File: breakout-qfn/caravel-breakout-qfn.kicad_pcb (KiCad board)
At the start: 2 copper layers, 45 x 57.5 mm, 83 parts, among them CON1 FH-00339, CON2 FH-00339, CON3 73251-1352, U1 Caravel_QFN

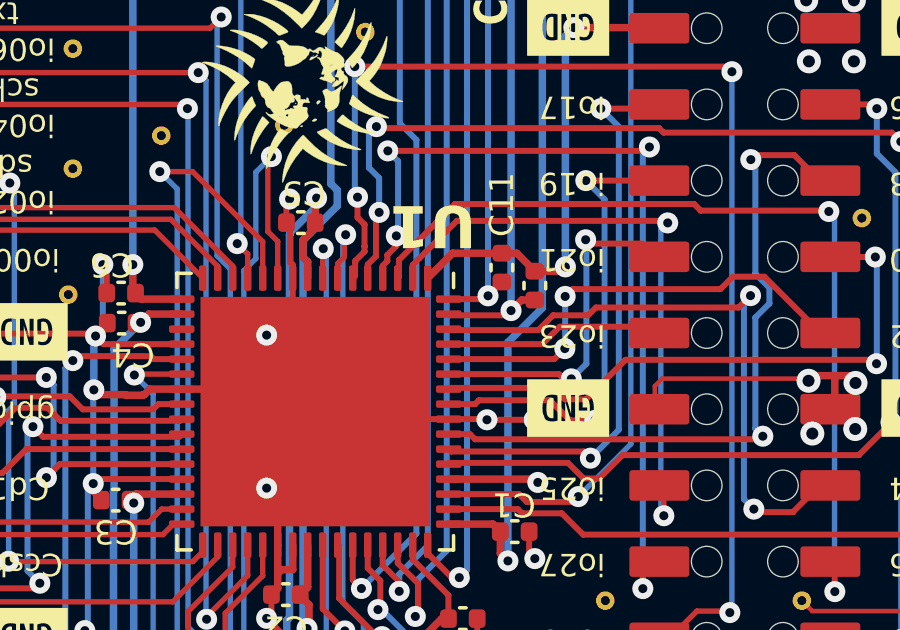
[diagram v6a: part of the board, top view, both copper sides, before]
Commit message: QFN breakout sanity naming for nets
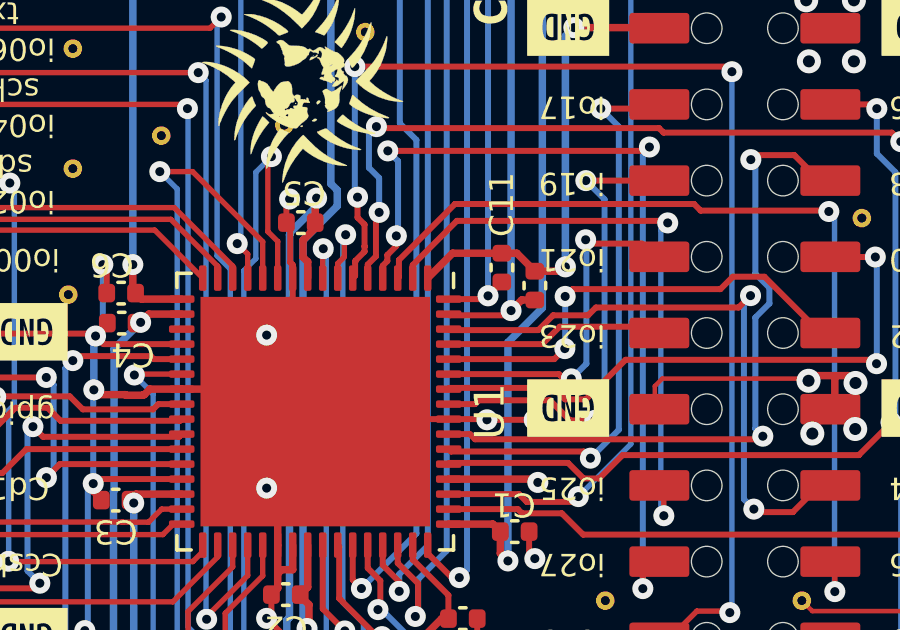
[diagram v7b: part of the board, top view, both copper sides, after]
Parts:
- CON1, CON2: value FH-00339 -> REF-182665-01
- U1: value Caravel_QFN -> Caravel_QFN_TT4; footprint Package_DFN_QFN:QFN-64-1EP_9x9mm_P0.5mm_EP7.65x7.65mm -> TinyTapeout:QFN-64-1EP_9x9mm_P0.5mm_EP7.65x7.65mm_REDUCEDPASTE
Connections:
- net mprj_io[0] renamed JTAG/mio[0]
- net mprj_io[10] renamed ui_in[2]/mio[10]
- net mprj_io[11] renamed ui_in[3]/mio[11]
- net mprj_io[12] renamed ui_in[4]/mio[12]
- net mprj_io[13] renamed ui_in[5]/mio[13]
- net mprj_io[14] renamed ui_in[6]/mio[14]
- net mprj_io[15] renamed ui_in[7]/mio[15]
- net mprj_io[16] renamed uo_out[0]/mio[16]
- net mprj_io[17] renamed uo_out[1]/mio[17]
- net mprj_io[18] renamed uo_out[2]/mio[18]
- net mprj_io[19] renamed uo_out[3]/mio[19]
- net mprj_io[1]_SDO renamed SDO/mio[1]
- net mprj_io[20] renamed uo_out[4]/mio[20]
- net mprj_io[21] renamed uo_out[5]/mio[21]
- net mprj_io[22] renamed uo_out[6]/mio[22]
- net mprj_io[23] renamed uo_out[7]/mio[23]
- net mprj_io[24] renamed uio[0]/mio[24]
- net mprj_io[25] renamed uio[1]/mio[25]
- net mprj_io[26] renamed uio[2]/mio[26]
- net mprj_io[27] renamed uio[3]/mio[27]
- net mprj_io[28] renamed uio[4]/mio[28]
- net mprj_io[29] renamed uio[5]/mio[29]
- net mprj_io[2]_SDI renamed SDI/mio[2]
- net mprj_io[30] renamed uio[6]/mio[30]
- net mprj_io[31] renamed uio[7]/mio[31]
- net mprj_io[32] renamed ctrl_ena/mio[32]
- net mprj_io[33] renamed mio[33]
- net mprj_io[34] renamed ctrl_sel_inc/mio[34]
- net mprj_io[35] renamed mio[35]
- net mprj_io[36] renamed ~{ctrl_sel_rst}/mio[36]
- net mprj_io[37] renamed mio[37]
- net mprj_io[3]_CSB renamed CSB/mio[3]
- net mprj_io[4]_SCK renamed SCK/mio[4]
- net mprj_io[5]_ser_rx renamed usrclk2/mio[5]
- net mprj_io[6]_ser_tx renamed clk/mio[6]
- net mprj_io[7] renamed ~{rst}/mio[7]
- net mprj_io[8] renamed ui_in[0]/mio[8]
- net mprj_io[9] renamed ui_in[1]/mio[9]

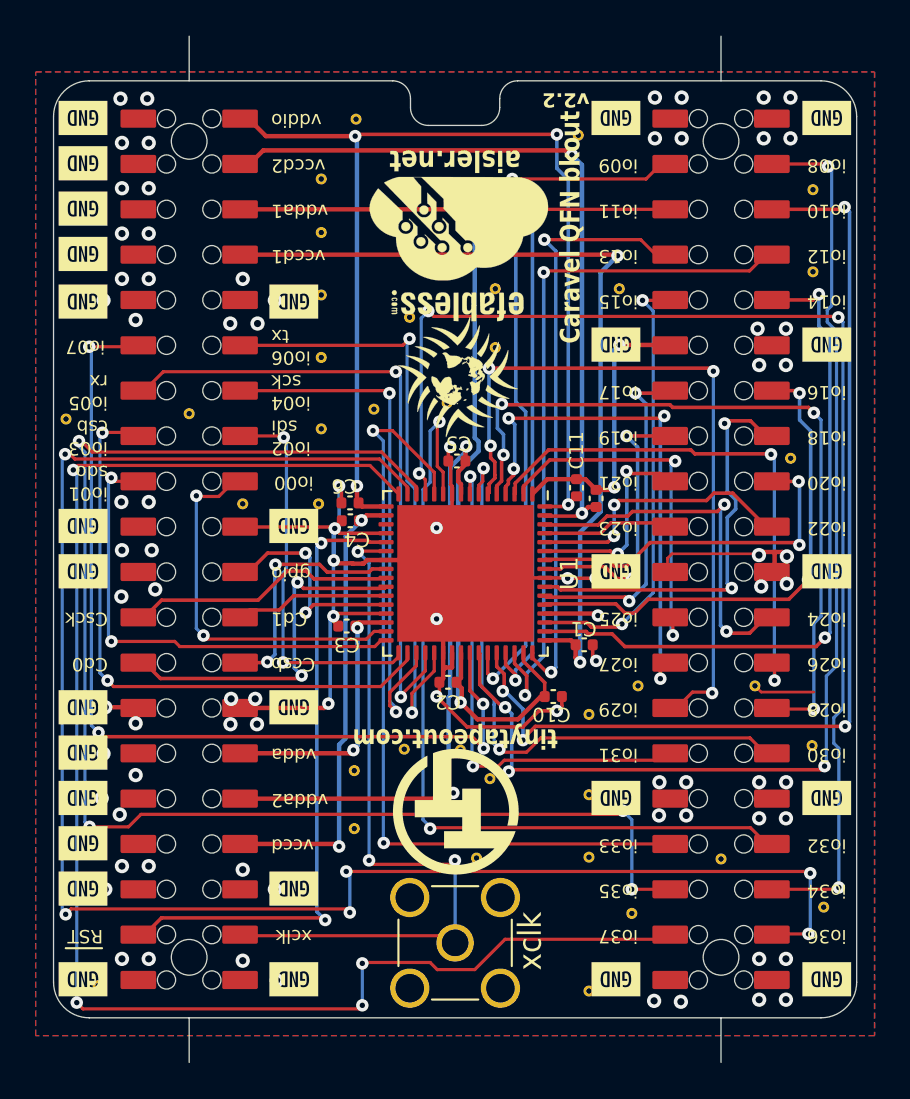
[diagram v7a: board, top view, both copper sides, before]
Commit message: v3.0, breaking changes for ultra-goodness: EMC,TT pinout, FPGA
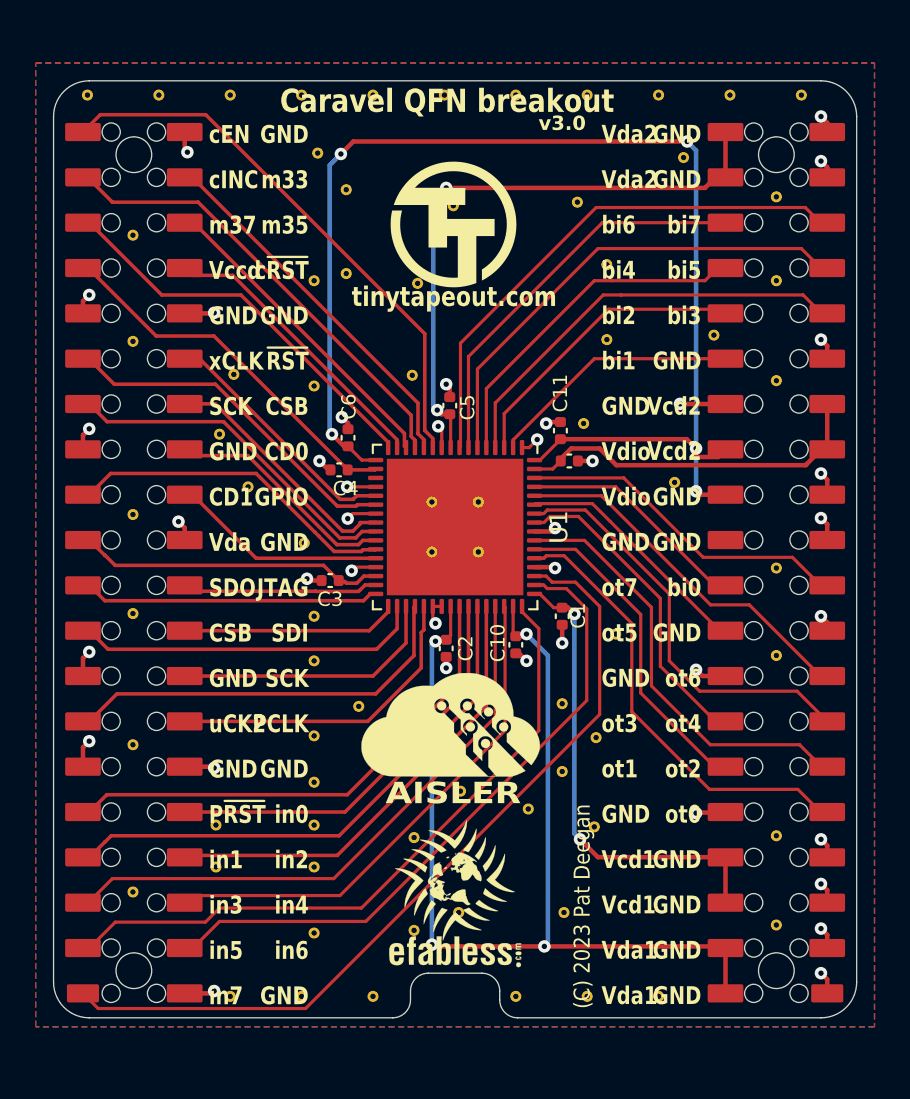
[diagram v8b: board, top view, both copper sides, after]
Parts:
- removed CON3: 73251-1352, ok-connectors:TE_5-1814832-2
- removed the REF** at (90.5, 54.8)
- removed the REF** at (72.8, 32.5)
- removed the REF** at (65.0, 19.6)
- removed the REF** at (63.0, 37.0)
- removed the REF** at (63.0, 33.0)
- removed the REF** at (50.5, 68.2)
- removed the REF** at (85.4, 61.1)
- removed the REF** at (64.8, 56.1)
- removed the REF** at (63.0, 26.0)
- removed the REF** at (67.7, 55.0)
- removed the REF** at (89.3, 38.6)
- removed the REF** at (90.5, 23.6)
- removed the REF** at (87.3, 51.4)
- removed the REF** at (90.5, 28.2)
- removed the REF** at (64.8, 59.4)
- removed the REF** at (48.7, 36.5)
- removed the REF** at (63.0, 23.0)
- removed the REF** at (55.6, 36.1)
- removed the REF** at (77.4, 20.6)
- removed the REF** at (78.0, 53.0)
- removed the REF** at (72.8, 29.1)
- removed the REF** at (80.4, 64.2)
- removed the REF** at (71.7, 61.0)
- removed the REF** at (78.0, 57.5)
- removed the REF** at (66.0, 35.9)
- removed the REF** at (62.9, 41.2)
- removed the REF** at (78.0, 68.5)
- removed the REF** at (68.0, 30.8)
- removed the REF** at (63.0, 29.5)
- removed the REF** at (80.8, 51.4)
- removed the REF** at (70.0, 35.5)
- removed the REF** at (79.7, 29.1)
- removed the REF** at (78.0, 61.0)
- removed the REF** at (58.6, 41.2)
- removed the REF** at (72.5, 56.6)
- removed the REF** at (72.8, 24.4)
- removed the REF** at (91.2, 63.8)
- removed the REF** at (70.8, 55.0)
- removed kibuzzard-6288F08E (x28): G***, kibuzzard-6288F08E
- added G***: LOGO, flyingcarsfootprints:PsychoLogoSmall, B.Cu at (70.5, 24.1)
- added REF**: Z2A_logo, Logos:Z2A_logo, B.Cu at (64.2, 58.7)
- added REF**: TT_logo, Logos:TT_logo, B.Cu at (78.8, 59.0)
- added STITCH1: StitchingVia-0.3mm, flyingcarsfootprints:StitchingVia-0.3mm, F.Cu at (69.2, 43.9)
- added STITCH1: StitchingVia-0.3mm, flyingcarsfootprints:StitchingVia-0.3mm, F.Cu at (76.6, 64.1)
- added STITCH1: StitchingVia-0.3mm, flyingcarsfootprints:StitchingVia-0.3mm, F.Cu at (78.3, 59.3)
- added STITCH1: StitchingVia-0.3mm, flyingcarsfootprints:StitchingVia-0.3mm, F.Cu at (71.8, 41.1)
- added STITCH1: StitchingVia-0.3mm, flyingcarsfootprints:StitchingVia-0.3mm, F.Cu at (70.7, 64.1)
- added STITCH1: StitchingVia-0.3mm, flyingcarsfootprints:StitchingVia-0.3mm, F.Cu at (83.3, 21.8)
- added STITCH1: StitchingVia-0.3mm, flyingcarsfootprints:StitchingVia-0.3mm, F.Cu at (70.4, 24.5)
- added STITCH1: StitchingVia-0.3mm, flyingcarsfootprints:StitchingVia-0.3mm, F.Cu at (69.2, 41.1)
- added STITCH1: StitchingVia-0.3mm, flyingcarsfootprints:StitchingVia-0.3mm, F.Cu at (49.9, 18.3)
- added STITCH1: StitchingVia-0.3mm, flyingcarsfootprints:StitchingVia-0.3mm, F.Cu at (71.8, 43.9)
- added STITCH1: StitchingVia-0.3mm, flyingcarsfootprints:StitchingVia-0.3mm, F.Cu at (64.4, 22.6)
- added STITCH10: StitchingVia-0.3mm, flyingcarsfootprints:StitchingVia-0.3mm, F.Cu at (85.9, 18.3)
- added STITCH11: StitchingVia-0.3mm, flyingcarsfootprints:StitchingVia-0.3mm, F.Cu at (89.9, 18.3)
- added STITCH12: StitchingVia-0.3mm, flyingcarsfootprints:StitchingVia-0.3mm, F.Cu at (61.9, 68.8)
- added STITCH13: StitchingVia-0.3mm, flyingcarsfootprints:StitchingVia-0.3mm, F.Cu at (65.9, 68.8)
- added STITCH15: StitchingVia-0.3mm, flyingcarsfootprints:StitchingVia-0.3mm, F.Cu at (73.9, 68.8)
- added STITCH16: StitchingVia-0.3mm, flyingcarsfootprints:StitchingVia-0.3mm, F.Cu at (77.9, 68.8)
- added STITCH17: StitchingVia-0.3mm, flyingcarsfootprints:StitchingVia-0.3mm, F.Cu at (74.6, 58.3)
- added STITCH17: StitchingVia-0.3mm, flyingcarsfootprints:StitchingVia-0.3mm, F.Cu at (52.5, 26.1)
- added STITCH17: StitchingVia-0.3mm, flyingcarsfootprints:StitchingVia-0.3mm, F.Cu at (77.3, 24.3)
- added STITCH17: StitchingVia-0.3mm, flyingcarsfootprints:StitchingVia-0.3mm, F.Cu at (68.4, 28.9)
- added STITCH17: StitchingVia-0.3mm, flyingcarsfootprints:StitchingVia-0.3mm, F.Cu at (78.4, 54.3)
- added STITCH17: StitchingVia-0.3mm, flyingcarsfootprints:StitchingVia-0.3mm, F.Cu at (68.2, 65.1)
- added STITCH17: StitchingVia-0.3mm, flyingcarsfootprints:StitchingVia-0.3mm, F.Cu at (76.5, 52.4)
- added STITCH17: StitchingVia-0.3mm, flyingcarsfootprints:StitchingVia-0.3mm, F.Cu at (68.1, 34.0)
- added STITCH17: StitchingVia-0.3mm, flyingcarsfootprints:StitchingVia-0.3mm, F.Cu at (58.9, 40.2)
- added STITCH17: StitchingVia-0.3mm, flyingcarsfootprints:StitchingVia-0.3mm, F.Cu at (62.6, 54.2)
- added STITCH17: StitchingVia-0.3mm, flyingcarsfootprints:StitchingVia-0.3mm, F.Cu at (52.5, 54.7)
- added STITCH17: StitchingVia-0.3mm, flyingcarsfootprints:StitchingVia-0.3mm, F.Cu at (70.8, 57.3)
- added STITCH17: StitchingVia-0.3mm, flyingcarsfootprints:StitchingVia-0.3mm, F.Cu at (52.5, 63.0)
- added STITCH17: StitchingVia-0.3mm, flyingcarsfootprints:StitchingVia-0.3mm, F.Cu at (79.0, 27.8)
- added STITCH17: StitchingVia-0.3mm, flyingcarsfootprints:StitchingVia-0.3mm, F.Cu at (74.4, 53.8)
- added STITCH17: StitchingVia-0.3mm, flyingcarsfootprints:StitchingVia-0.3mm, F.Cu at (57.1, 59.2)
- added STITCH17: StitchingVia-0.3mm, flyingcarsfootprints:StitchingVia-0.3mm, F.Cu at (62.6, 56.8)
- added STITCH17: StitchingVia-0.3mm, flyingcarsfootprints:StitchingVia-0.3mm, F.Cu at (88.5, 64.8)
- added STITCH17: StitchingVia-0.3mm, flyingcarsfootprints:StitchingVia-0.3mm, F.Cu at (52.5, 47.4)
- added STITCH17: StitchingVia-0.3mm, flyingcarsfootprints:StitchingVia-0.3mm, F.Cu at (88.5, 59.8)
- added STITCH17: StitchingVia-0.3mm, flyingcarsfootprints:StitchingVia-0.3mm, F.Cu at (52.5, 32.1)
- added STITCH17: StitchingVia-0.3mm, flyingcarsfootprints:StitchingVia-0.3mm, F.Cu at (88.5, 49.7)
- added STITCH17: StitchingVia-0.3mm, flyingcarsfootprints:StitchingVia-0.3mm, F.Cu at (68.2, 59.9)
- added STITCH17: StitchingVia-0.3mm, flyingcarsfootprints:StitchingVia-0.3mm, F.Cu at (62.6, 34.6)
- added STITCH17: StitchingVia-0.3mm, flyingcarsfootprints:StitchingVia-0.3mm, F.Cu at (62.6, 61.5)
- added STITCH17: StitchingVia-0.3mm, flyingcarsfootprints:StitchingVia-0.3mm, F.Cu at (62.6, 59.2)
- added STITCH17: StitchingVia-0.3mm, flyingcarsfootprints:StitchingVia-0.3mm, F.Cu at (62.6, 47.5)
- added STITCH17: StitchingVia-0.3mm, flyingcarsfootprints:StitchingVia-0.3mm, F.Cu at (65.1, 52.5)
- added STITCH17: StitchingVia-0.3mm, flyingcarsfootprints:StitchingVia-0.3mm, F.Cu at (77.7, 36.7)
- added STITCH17: StitchingVia-0.3mm, flyingcarsfootprints:StitchingVia-0.3mm, F.Cu at (82.8, 40.0)
- added STITCH17: StitchingVia-0.3mm, flyingcarsfootprints:StitchingVia-0.3mm, F.Cu at (62.6, 50.0)
- added STITCH17: StitchingVia-0.3mm, flyingcarsfootprints:StitchingVia-0.3mm, F.Cu at (64.4, 28.3)
- added STITCH17: StitchingVia-0.3mm, flyingcarsfootprints:StitchingVia-0.3mm, F.Cu at (79.0, 32.0)
- added STITCH17: StitchingVia-0.3mm, flyingcarsfootprints:StitchingVia-0.3mm, F.Cu at (58.1, 34.0)
- added STITCH17: StitchingVia-0.3mm, flyingcarsfootprints:StitchingVia-0.3mm, F.Cu at (88.5, 24.0)
- added STITCH17: StitchingVia-0.3mm, flyingcarsfootprints:StitchingVia-0.3mm, F.Cu at (79.5, 48.5)
- added STITCH17: StitchingVia-0.3mm, flyingcarsfootprints:StitchingVia-0.3mm, F.Cu at (88.5, 34.3)
- added STITCH17: StitchingVia-0.3mm, flyingcarsfootprints:StitchingVia-0.3mm, F.Cu at (62.8, 21.6)
- added STITCH17: StitchingVia-0.3mm, flyingcarsfootprints:StitchingVia-0.3mm, F.Cu at (57.1, 61.5)
- added STITCH17: StitchingVia-0.3mm, flyingcarsfootprints:StitchingVia-0.3mm, F.Cu at (52.5, 41.8)
- added STITCH17: StitchingVia-0.3mm, flyingcarsfootprints:StitchingVia-0.3mm, F.Cu at (88.5, 44.8)
- added STITCH17: StitchingVia-0.3mm, flyingcarsfootprints:StitchingVia-0.3mm, F.Cu at (85.0, 31.8)
- added STITCH17: StitchingVia-0.3mm, flyingcarsfootprints:StitchingVia-0.3mm, F.Cu at (57.3, 37.3)
- added STITCH17: StitchingVia-0.3mm, flyingcarsfootprints:StitchingVia-0.3mm, F.Cu at (76.5, 56.2)
- added STITCH17: StitchingVia-0.3mm, flyingcarsfootprints:StitchingVia-0.3mm, F.Cu at (62.6, 28.7)
- added STITCH17: StitchingVia-0.3mm, flyingcarsfootprints:StitchingVia-0.3mm, F.Cu at (81.9, 68.8)
- added STITCH17: StitchingVia-0.3mm, flyingcarsfootprints:StitchingVia-0.3mm, F.Cu at (62.6, 65.2)
- added STITCH17: StitchingVia-0.3mm, flyingcarsfootprints:StitchingVia-0.3mm, F.Cu at (88.5, 28.7)
- added STITCH17: StitchingVia-0.3mm, flyingcarsfootprints:StitchingVia-0.3mm, F.Cu at (62.0, 43.4)
- added STITCH17: StitchingVia-0.3mm, flyingcarsfootprints:StitchingVia-0.3mm, F.Cu at (68.2, 52.4)
- added STITCH2: StitchingVia-0.3mm, flyingcarsfootprints:StitchingVia-0.3mm, F.Cu at (53.9, 18.3)
- added STITCH3: StitchingVia-0.3mm, flyingcarsfootprints:StitchingVia-0.3mm, F.Cu at (57.9, 18.3)
- added STITCH3: StitchingVia-0.3mm, flyingcarsfootprints:StitchingVia-0.3mm, F.Cu at (57.9, 68.8)
- added STITCH4: StitchingVia-0.3mm, flyingcarsfootprints:StitchingVia-0.3mm, F.Cu at (61.9, 18.3)
- added STITCH5: StitchingVia-0.3mm, flyingcarsfootprints:StitchingVia-0.3mm, F.Cu at (65.9, 18.3)
- added STITCH6: StitchingVia-0.3mm, flyingcarsfootprints:StitchingVia-0.3mm, F.Cu at (69.9, 18.3)
- added STITCH7: StitchingVia-0.3mm, flyingcarsfootprints:StitchingVia-0.3mm, F.Cu at (73.9, 18.3)
- added STITCH8: StitchingVia-0.3mm, flyingcarsfootprints:StitchingVia-0.3mm, F.Cu at (77.9, 18.3)
- added STITCH9: StitchingVia-0.3mm, flyingcarsfootprints:StitchingVia-0.3mm, F.Cu at (81.9, 18.3)
- moved REF** 36.2 mm to (70.5, 66.3), turned to 0 degrees
- moved REF** 33.6 mm to (70.5, 56.5), turned to 0 degrees
- moved REF** 32.8 mm to (70.5, 25.6), turned to 0 degrees
- moved REF** 28.2 mm to (70.5, 62.3), turned to 0 degrees
- moved C6 3.65 mm to (64.5, 37.5), turned to -90 degrees
- moved C10 3.58 mm to (73.9, 49.1), turned to -90 degrees
- moved C11 3.32 mm to (76.4, 37.1)
- moved CON1 3.19 mm to (52.5, 44.5)
- moved CON2 3.19 mm to (88.5, 44.5)
- moved C5 3.13 mm to (70.2, 35.7), turned to -90 degrees
- moved C4 2.92 mm to (64.0, 39.3)
- moved C3 2.71 mm to (63.5, 45.5)
- moved U1 2.66 mm to (70.5, 42.5)
- moved C7 2.58 mm to (76.9, 38.8), turned to 180 degrees
- moved C1 2.02 mm to (76.5, 47.5), turned to 90 degrees
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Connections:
- CON1 pad 1: GND -> ctrl_ena/mio[32]
- CON1 pad 11: ~{rst}/mio[7] -> xclk
- CON1 pad 12: clk/mio[6] -> ~{RST}
- CON1 pad 13: usrclk2/mio[5] -> Caravel_SCK
- CON1 pad 14: SCK/mio[4] -> Caravel_CSB
- CON1 pad 15: CSB/mio[3] -> GND
- CON1 pad 16: SDI/mio[2] -> Caravel_D0
- CON1 pad 17: SDO/mio[1] -> Caravel_D1
- CON1 pad 18: JTAG/mio[0] -> gpio
- CON1 pad 19: GND -> vdda
- CON1 pad 2: vddio -> GND
- CON1 pad 21: GND -> SDO/mio[1]
- CON1 pad 22: gpio -> JTAG/mio[0]
- CON1 pad 23: Caravel_SCK -> CSB/mio[3]
- CON1 pad 24: Caravel_D1 -> SDI/mio[2]
- CON1 pad 25: Caravel_D0 -> GND
- CON1 pad 26: Caravel_CSB -> SCK/mio[4]
- CON1 pad 27: GND -> usrclk2/mio[5]
- CON1 pad 28: GND -> clk/mio[6]
- CON1 pad 3: GND -> ctrl_sel_inc/mio[34]
- CON1 pad 30: vdda -> GND
- CON1 pad 31: GND -> ~{rst}/mio[7]
- CON1 pad 32: vdda2 -> ui_in[0]/mio[8]
- CON1 pad 33: GND -> ui_in[1]/mio[9]
- CON1 pad 34: vccd -> ui_in[2]/mio[10]
- CON1 pad 35: GND -> ui_in[3]/mio[11]
- CON1 pad 36: GND -> ui_in[4]/mio[12]
- CON1 pad 37: ~{RST} -> ui_in[5]/mio[13]
- CON1 pad 38: xclk -> ui_in[6]/mio[14]
- CON1 pad 39: GND -> ui_in[7]/mio[15]
- CON1 pad 4: vccd2 -> mio[33]
- CON1 pad 5: GND -> mio[37]
- CON1 pad 6: vdda1 -> mio[35]
- CON1 pad 7: GND -> vccd
- CON1 pad 8: vccd1 -> ~{ctrl_sel_rst}/mio[36]
- CON2 pad 1: GND -> vdda2
- CON2 pad 10: ui_in[6]/mio[14] -> uio[3]/mio[27]
- CON2 pad 11: GND -> uio[1]/mio[25]
- CON2 pad 13: uo_out[1]/mio[17] -> GND
- CON2 pad 14: uo_out[0]/mio[16] -> vccd2
- CON2 pad 15: uo_out[3]/mio[19] -> vddio
- CON2 pad 16: uo_out[2]/mio[18] -> vccd2
- CON2 pad 17: uo_out[5]/mio[21] -> vddio
- CON2 pad 18: uo_out[4]/mio[20] -> GND
- CON2 pad 19: uo_out[7]/mio[23] -> GND
- CON2 pad 20: uo_out[6]/mio[22] -> GND
- CON2 pad 21: GND -> uo_out[7]/mio[23]
- CON2 pad 22: GND -> uio[0]/mio[24]
- CON2 pad 23: uio[1]/mio[25] -> uo_out[5]/mio[21]
- CON2 pad 24: uio[0]/mio[24] -> GND
- CON2 pad 25: uio[3]/mio[27] -> GND
- CON2 pad 26: uio[2]/mio[26] -> uo_out[6]/mio[22]
- CON2 pad 27: uio[5]/mio[29] -> uo_out[3]/mio[19]
- CON2 pad 28: uio[4]/mio[28] -> uo_out[4]/mio[20]
- CON2 pad 29: uio[7]/mio[31] -> uo_out[1]/mio[17]
- CON2 pad 3: ui_in[1]/mio[9] -> vdda2
- CON2 pad 30: uio[6]/mio[30] -> uo_out[2]/mio[18]
- CON2 pad 32: GND -> uo_out[0]/mio[16]
- CON2 pad 33: mio[33] -> vccd1
- CON2 pad 34: ctrl_ena/mio[32] -> GND
- CON2 pad 35: mio[35] -> vccd1
- CON2 pad 36: ctrl_sel_inc/mio[34] -> GND
- CON2 pad 37: mio[37] -> vdda1
- CON2 pad 38: ~{ctrl_sel_rst}/mio[36] -> GND
- CON2 pad 39: GND -> vdda1
- CON2 pad 4: ui_in[0]/mio[8] -> GND
- CON2 pad 5: ui_in[3]/mio[11] -> uio[6]/mio[30]
- CON2 pad 6: ui_in[2]/mio[10] -> uio[7]/mio[31]
- CON2 pad 7: ui_in[5]/mio[13] -> uio[4]/mio[28]
- CON2 pad 8: ui_in[4]/mio[12] -> uio[5]/mio[29]
- CON2 pad 9: ui_in[7]/mio[15] -> uio[2]/mio[26]
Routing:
- net ~{ctrl_sel_rst}/mio[36]: track 96.3 -> 16.3 mm, vias 6 -> 0
- net mio[37]: track 85.6 -> 22.5 mm, vias 4 -> 0
- net mio[35]: track 79.1 -> 18.0 mm, vias 4 -> 0
- net GND: track 104.5 -> 49.0 mm, vias 87 -> 39
- net ctrl_sel_inc/mio[34]: track 69.8 -> 25.8 mm, vias 4 -> 0
- net ui_in[0]/mio[8]: track 62.7 -> 23.4 mm, vias 4 -> 0
- net ui_in[2]/mio[10]: track 57.3 -> 26.0 mm, vias 4 -> 0
- net mio[33]: track 44.9 -> 20.9 mm, vias 2 -> 0
- net ~{rst}/mio[7]: track 52.1 -> 28.4 mm, vias 4 -> 0
- net uio[4]/mio[28]: track 42.3 -> 19.5 mm, vias 4 -> 0
- net ~{RST}: track 36.2 -> 14.0 mm, vias 2 -> 0
- net vccd2: track 42.1 -> 20.2 mm, vias 2 -> 0
- net ui_in[7]/mio[15]: track 25.0 -> 46.5 mm, vias 2 -> 0
- net vccd1: track 47.6 -> 26.6 mm
- net xclk: track 40.9 -> 19.9 mm, vias 3 -> 0
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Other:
- board size 45 x 57.5 mm -> 45 x 52.5 mm
- board text added: "(C) 2023 Pat Deegan"
- board text added: "(C) 2023 Pat Deegan https://psychogenic.com"
- board text added: "AISLER"
- board text added: "CD0"
- board text added: "CD1"
- board text added: "CSB"
- board text added: "Caravel QFN breakout"
- board text added: "Caravel QFN breakout v3"
- board text added: "GND"
- board text added: "GPIO"
- board text added: "JTAG"
- board text added: "PCLK"
- board text added: "P~{RST}"
- board text added: "SCK"
- board text added: "SDI"
- board text added: "SDO"
- board text added: "TinyTapeout projects are packaged together within Caravel, an SoC that provides space for user projects, pads to connect to the outside world and other features like a microcontroller, logic analyzer, etc. This PCB provides a way to deliver these chips that will sit atop the demo board, but also allows you to easily integrate the ICs into your own projects. For details, see"
- board text added: "Vccd"
- board text added: "Vcd1"
- board text added: "Vcd2"
- board text added: "Vda"
- board text added: "Vda1"
- board text added: "Vda2"
- board text added: "Vdio"
- board text added: "bi0"
- board text added: "bi1"
- board text added: "bi2"
- board text added: "bi3"
- board text added: "bi4"
- board text added: "bi5"
- board text added: "bi6"
- board text added: "bi7"
- board text added: "cEN"
- board text added: "cINC"
- board text added: "c~{RST}"
- board text added: "https://github.com/TinyTapeout/caravel-breakout-pcb"
- board text added: "in0"
- board text added: "in1"
- board text added: "in2"
- board text added: "in3"
- board text added: "in4"
- board text added: "in5"
- board text added: "in6"
- board text added: "in7"
- board text added: "m33"
- board text added: "m35"
- board text added: "m37"
- board text added: "ot0"
- board text added: "ot1"
- board text added: "ot2"
- board text added: "ot3"
- board text added: "ot4"
- board text added: "ot5"
- board text added: "ot6"
- board text added: "ot7"
- board text added: "uCK2"
- board text added: "v3.0"
- board text added: "xCLK"
- board text added: "zerotoasiccourse.com"
- board text added: "~{RST}"
- board text removed: "Caravel QFN bkout"
- board text removed: "Ccsb"
- board text removed: "Cd0"
- board text removed: "Cd1"
- board text removed: "Csck"
- board text removed: "RST"
- board text removed: "aisler.net"
- board text removed: "gpio"
- board text removed: "io00"
- board text removed: "io01 sdo"
- board text removed: "io02 sdi"
- board text removed: "io03 csb"
- board text removed: "io04 sck"
- board text removed: "io05 rx"
- board text removed: "io06 tx"
- board text removed: "io07"
- board text removed: "io08"
- board text removed: "io09"
- board text removed: "io10"
- board text removed: "io11"
- board text removed: "io12"
- board text removed: "io13"
- board text removed: "io14"
- board text removed: "io15"
- board text removed: "io16"
- board text removed: "io17"
- board text removed: "io18"
- board text removed: "io19"
- board text removed: "io20"
- board text removed: "io21"
- board text removed: "io22"
- board text removed: "io23"
- board text removed: "io24"
- board text removed: "io25"
- board text removed: "io26"
- board text removed: "io27"
- board text removed: "io28"
- board text removed: "io29"
- board text removed: "io30"
- board text removed: "io31"
- board text removed: "io32"
- board text removed: "io33"
- board text removed: "io34"
- board text removed: "io35"
- board text removed: "io36"
- board text removed: "io37"
- board text removed: "v2.2"
- board text removed: "vccd"
- board text removed: "vccd1"
- board text removed: "vccd2"
- board text removed: "vdda"
- board text removed: "vdda1"
- board text removed: "vdda2"
- board text removed: "vddio"
- board text removed: "xclk"
